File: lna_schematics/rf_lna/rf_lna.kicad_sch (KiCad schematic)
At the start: 18 parts, among them J1 Conn_Coaxial_Small, J2 Conn_Coaxial_Small, U2 BFP640

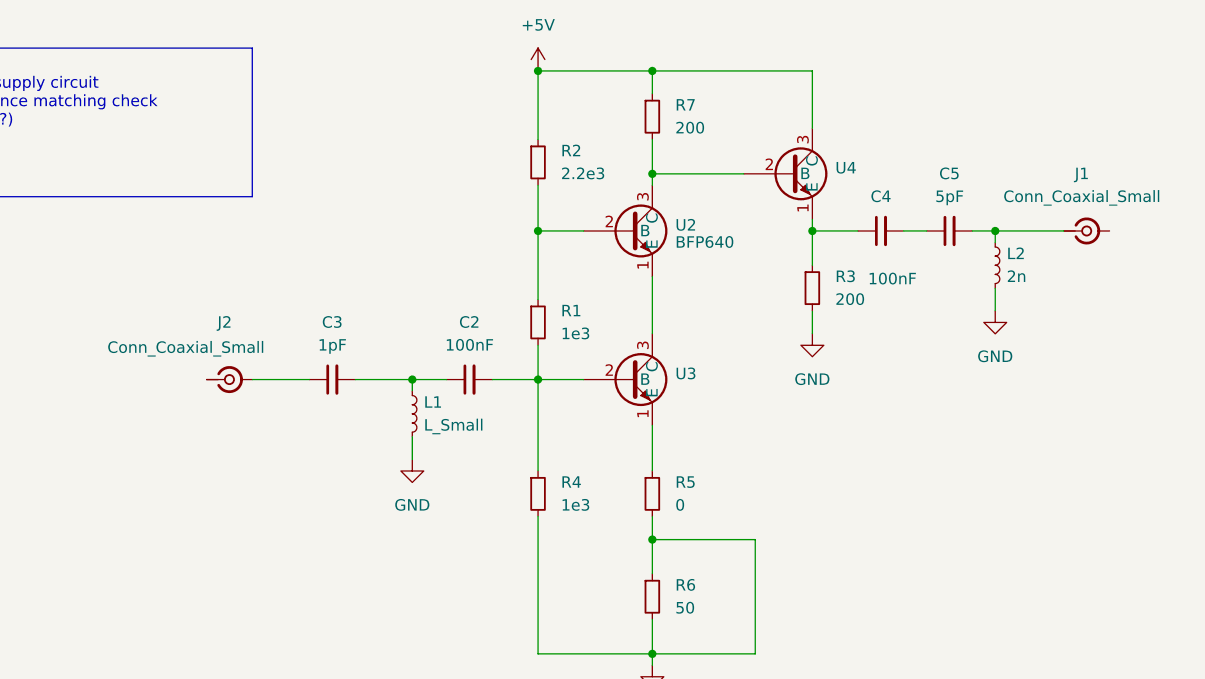
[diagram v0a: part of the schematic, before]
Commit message: [simulations] Added L-matching networks | TODO: find wide-band matching T / Pi matching circuits (800MHz -> 1.5 GHz), find actual working components for the circuit
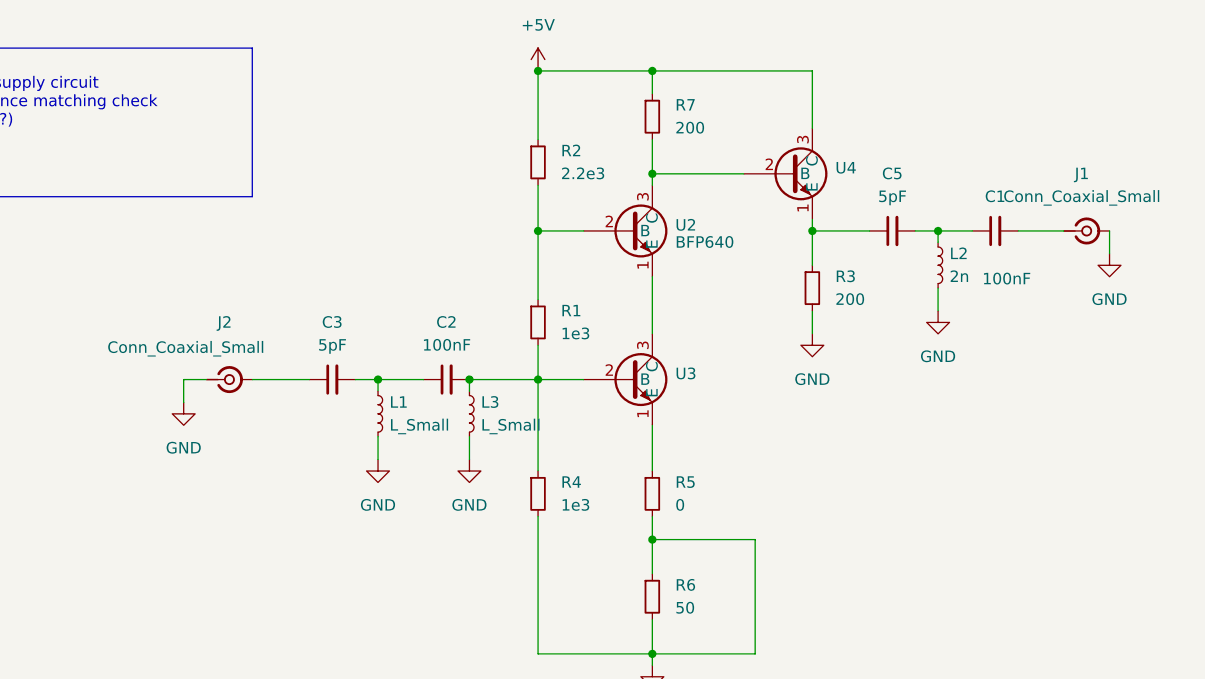
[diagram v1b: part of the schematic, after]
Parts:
- removed C4: 100nF, symbol Device:C_Small
- added C1: 100nF, symbol Device:C_Small
- added L3: L_Small, symbol Device:L_Small
- C3: value 1pF -> 5pF
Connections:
- net GND: now also J1.2 (Ext), J2.1 (In), L3.2
- net at C2.2, R1.2, R4.1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: now also L3.1
- net at R3.1, U4.1 (E): now also C5.1
- net at C5.2, L2.1: now also C1.1; no longer J1.1 (In)
- new net: C1.2, J1.1 (In)
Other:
- moved on the sheet: C2, C5, L1, L2

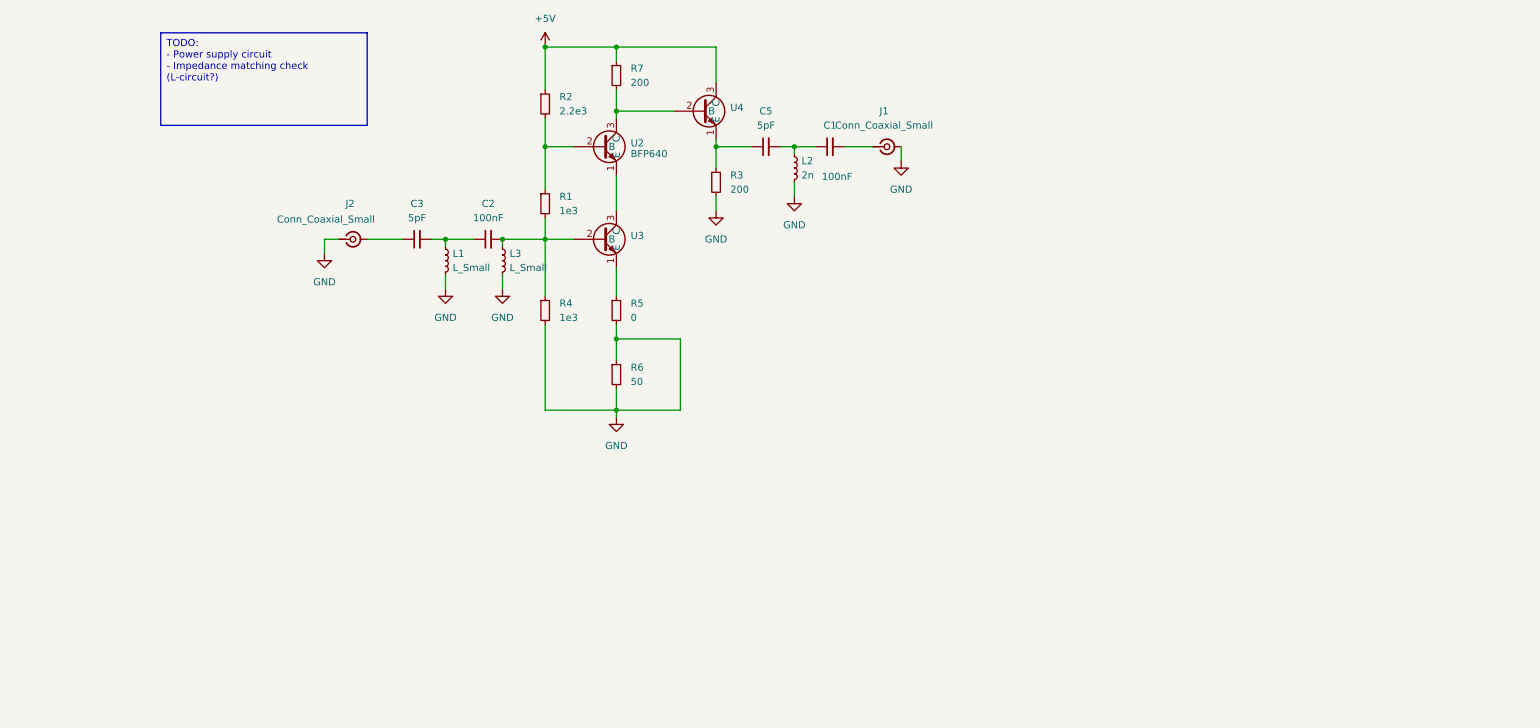
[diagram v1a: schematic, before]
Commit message: [lna_schematics] Simulated with matched impedance to get voltage values and verify matching parameters [lna_schematics] Added matched elements, added notes
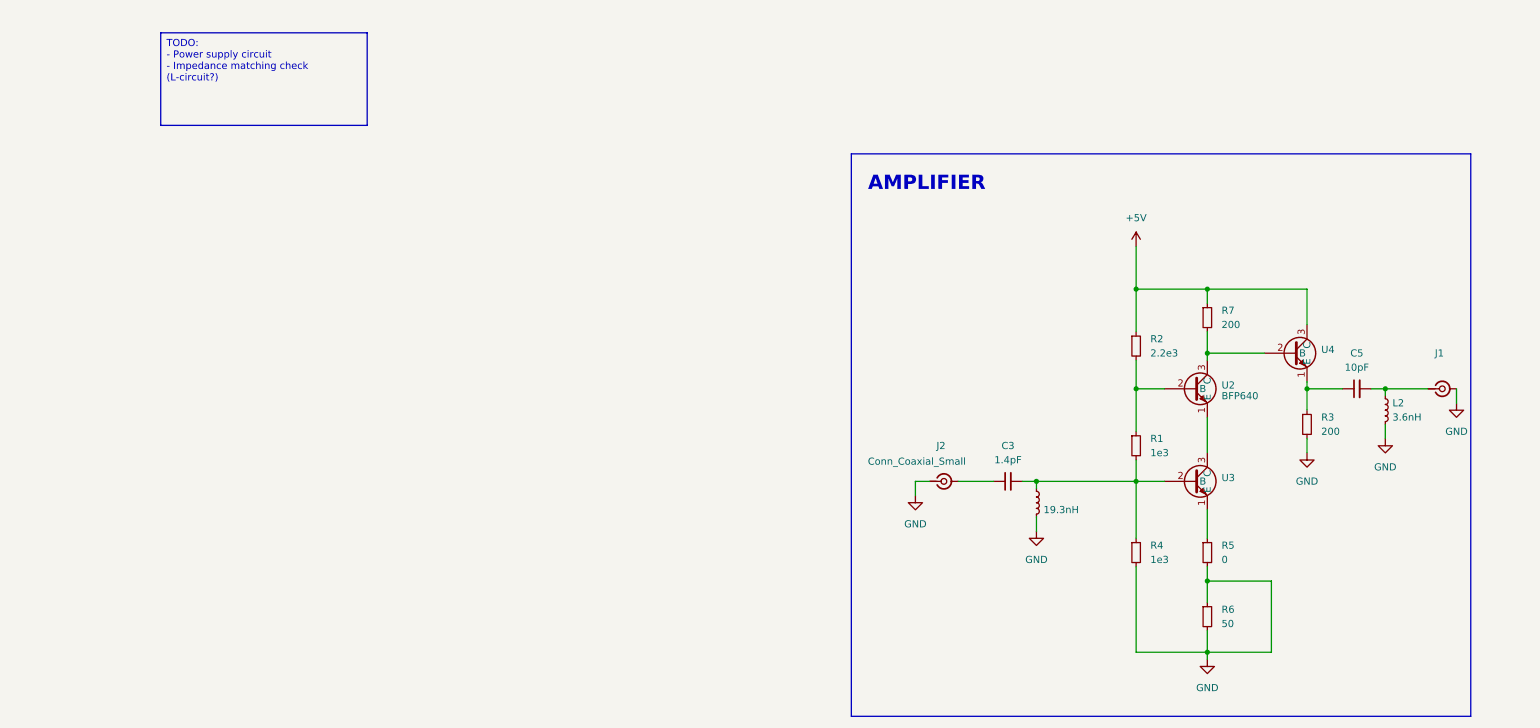
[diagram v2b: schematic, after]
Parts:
- removed C1, C2: 100nF, symbol Device:C_Small
- removed L3: L_Small, symbol Device:L_Small
- C3: value 5pF -> 1.4pF
- C5: value 5pF -> 10pF
- L1: value L_Small -> 19.3nH
- L2: value 2n -> 3.6nH
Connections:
- net at C3.2, L1.1: now also R1.2, R4.1, U3.2 (B)
- net at C5.2, L2.1: now also J1.1 (In)
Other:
- note added: "AMPLIFIER"
- moved on the sheet: C3, C5, J1, J2, L2, R1, R2, R3, R4, R5, R6, R7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

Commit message: [kicad] Added various footprints, added matched network
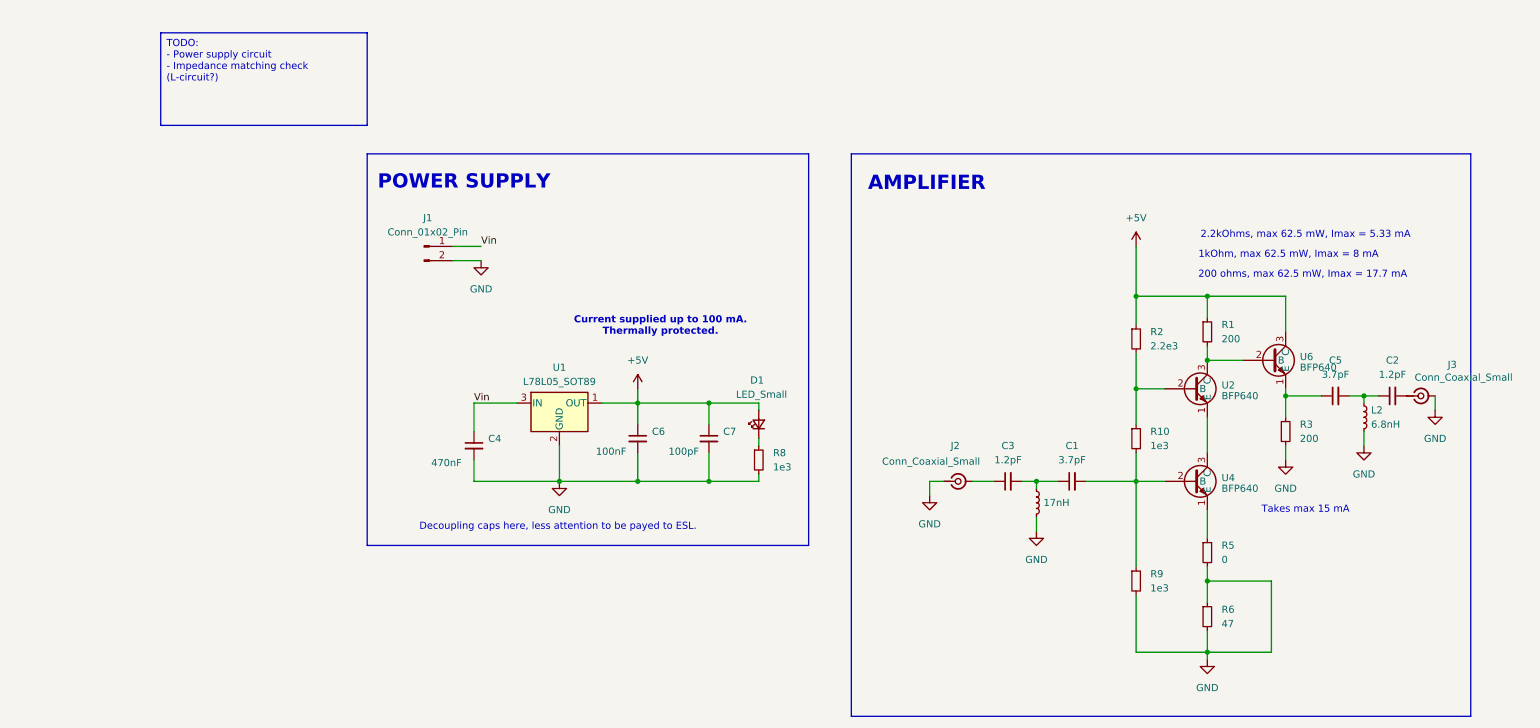
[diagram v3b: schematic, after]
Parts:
- removed J1: Conn_Coaxial_Small, symbol Connector:Conn_Coaxial_Small
- removed R4: 1e3, symbol Device:R_Small
- removed R7: 200, symbol Device:R_Small
- removed U3: ~, symbol rf_lna:BFP640
- added C1: 3.7pF, symbol Device:C_Small
- added C2: 1.2pF, Capacitor_SMD:C_0402_1005Metric, symbol Device:C_Small
- added C4: 470nF, Capacitor_SMD:C_0603_1608Metric, symbol Device:C_Small
- added C6: 100nF, Capacitor_SMD:C_0402_1005Metric, symbol Device:C_Small
- added C7: 100pF, Capacitor_SMD:C_0402_1005Metric, symbol Device:C_Small
- added D1: LED_Small, LED_SMD:LED_0603_1608Metric, symbol Device:LED_Small
- added J1: Conn_01x02_Pin, Connector_Wire:SolderWire-0.25sqmm_1x02_P4.2mm_D0.65mm_OD1.7mm, symbol Connector:Conn_01x02_Pin
- added J3: Conn_Coaxial_Small, Connector_Coaxial:SMA_BAT_Wireless_BWSMA-KWE-Z001, symbol Connector:Conn_Coaxial_Small
- added R10, R8, R9: 1e3, Resistor_SMD:R_0402_1005Metric, symbol Device:R_Small
- added U1: L78L05_SOT89, Package_TO_SOT_SMD:SOT-89-3, symbol Regulator_Linear:L78L05_SOT89
- added U6: BFP640, Library:BFP640, symbol rf_lna:BFP640
- C3: value 1.4pF -> 1.2pF; footprint (none) -> Capacitor_SMD:C_0402_1005Metric; LCSC Part Number (none) -> C76899; Manufacturing Part Number (none) -> GJM1555C1H1R2WB01D
- C5: value 10pF -> 3.7pF
- J2: footprint (none) -> Connector_Coaxial:SMA_BAT_Wireless_BWSMA-KWE-Z001; LCSC Part Number (none) -> C496549; Manufacturing Part Number (none) -> BWSMA-KE-Z001
- L1: value 19.3nH -> 17nH
- L2: value 3.6nH -> 6.8nH
- R1: value 1e3 -> 200; footprint (none) -> Resistor_SMD:R_0402_1005Metric; LCSC Part Number (none) -> C25091; Manufacturing Part Number (none) -> 0402WGF2200TCE
- R2: footprint (none) -> Resistor_SMD:R_0402_1005Metric; LCSC Part Number (none) -> C25879; Manufacturing Part Number (none) -> 0402WGF2201TCE
- R3: footprint (none) -> Resistor_SMD:R_0402_1005Metric; LCSC Part Number (none) -> C25091; Manufacturing Part Number (none) -> 0402WGF2200TCE
- R5: footprint (none) -> Capacitor_SMD:C_0402_1005Metric; LCSC Part Number (none) -> C17168; Manufacturing Part Number (none) -> 0402WGF0000TCE
- R6: value 50 -> 47; footprint (none) -> Capacitor_SMD:C_0402_1005Metric; LCSC Part Number (none) -> C4109; Manufacturing Part Number (none) -> 0402WGF2001TCE
- U2: footprint (none) -> Library:BFP640; LCSC Part Number (none) -> C439781; MFR.Part BFP640H6327 -> (none); Manufacturing Part Number (none) -> BFP640H6327; jlcpcb C439781 -> (none)
- U4: value ~ -> BFP640; footprint (none) -> Library:BFP640; LCSC Part Number (none) -> C439781; Manufacturing Part Number (none) -> BFP640H6327
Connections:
- net +5V: now also R1.1, C6.1, C7.1, D1.2 (A), U1.1 (OUT), U6.3 (C); no longer U4.3 (C)
- net GND: now also C4.2, C6.2, C7.2, J1.2 (Pin_2), J3.2 (Ext), R8.2, R9.2, U1.2 (GND)
- net at C3.2, L1.1: now also C1.1; no longer R1.2
- net at C5.1, R3.1: now also U6.1 (E); no longer U4.1 (E)
- net at U4.2 (B): now also C1.2, R10.2, R9.1; no longer U2.3 (C)
- net at R5.1: now also U4.1 (E)
- net at C5.2, L2.1: now also C2.1
- net at R2.2, U2.2 (B): now also R10.1; no longer R1.1
- net at U2.1 (E): now also U4.3 (C)
- new net: D1.1 (K), R8.1
- new net: C2.2, J3.1 (In)
- new net: R1.2, U2.3 (C), U6.2 (B)
- new net Vin: C4.1, J1.1 (Pin_1), U1.3 (IN)
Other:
- note added: "1kOhm, max 62.5 mW, Imax = 8 mA"
- note added: "2.2kOhms, max 62.5 mW, Imax = 5.33 mA"
- note added: "200 ohms, max 62.5 mW, Imax = 17.7 mA"
- note added: "Current supplied up to 100 mA. Thermally protected."
- note added: "Decoupling caps here, less attention to be payed to ESL."
- note added: "POWER SUPPLY"
- note added: "Takes max 15 mA"
- moved on the sheet: C5, J2, L2, R2, R3

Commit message: [lna_schematics] added final components for impedance matching [simulations] Added final impedance matched simulations | TODO: stackup + layout + footprint check
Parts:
- C1, C5: footprint (none) -> Capacitor_SMD:C_0402_1005Metric; LCSC Part Number (none) -> C161321; Manufacturing Part Number (none) -> GJM1555C1H3R6WB01D
- L1: value 17nH -> 18nH; footprint (none) -> Inductor_SMD:L_0402_1005Metric; LCSC Part Number (none) -> C24562; Manufacturing Part Number (none) -> SDCL1005C18NJTDF
- L2: footprint (none) -> Inductor_SMD:L_0402_1005Metric; LCSC Part Number (none) -> C32041; Manufacturing Part Number (none) -> SDCL1005C6N8JTDF

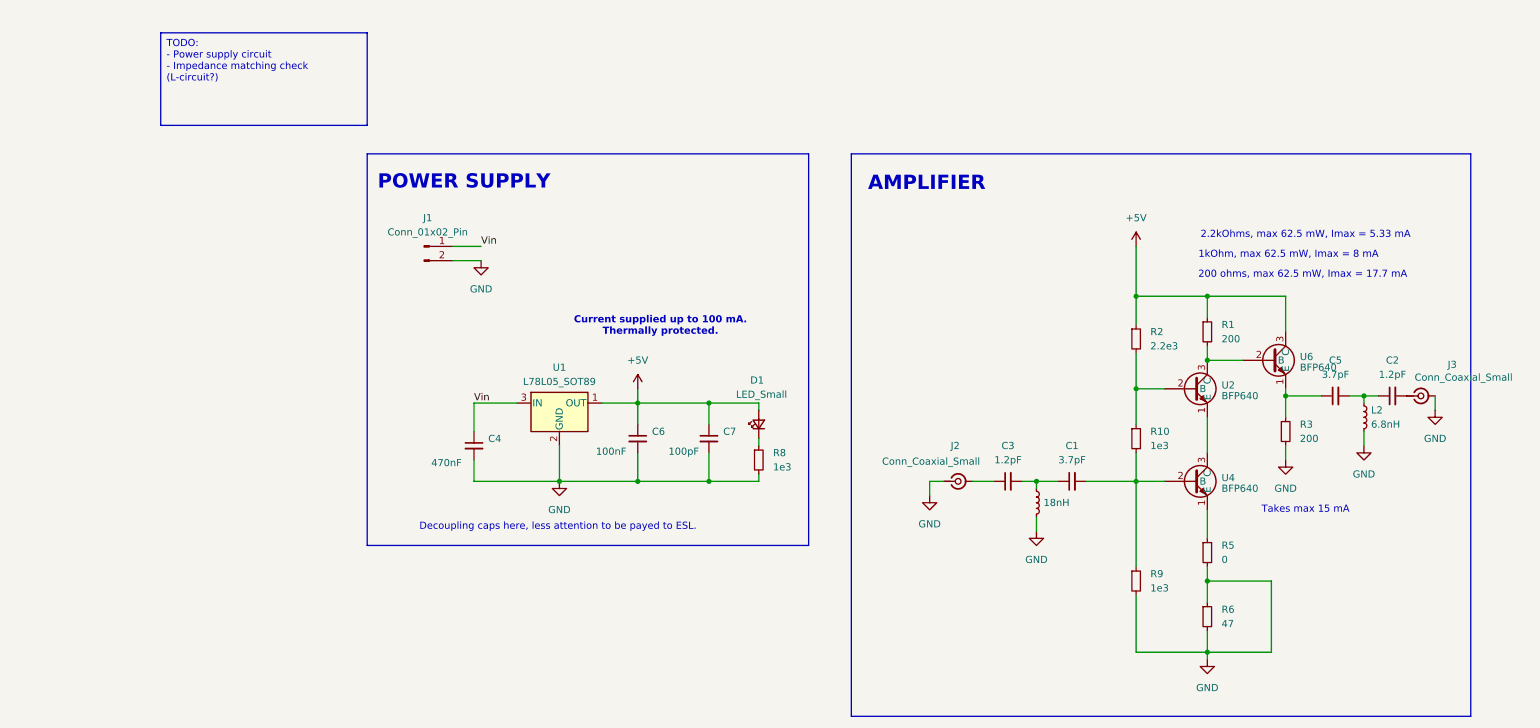
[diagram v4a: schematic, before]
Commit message: [kicad] Finished pads, stackup, symbols for LNA. Starting layout.
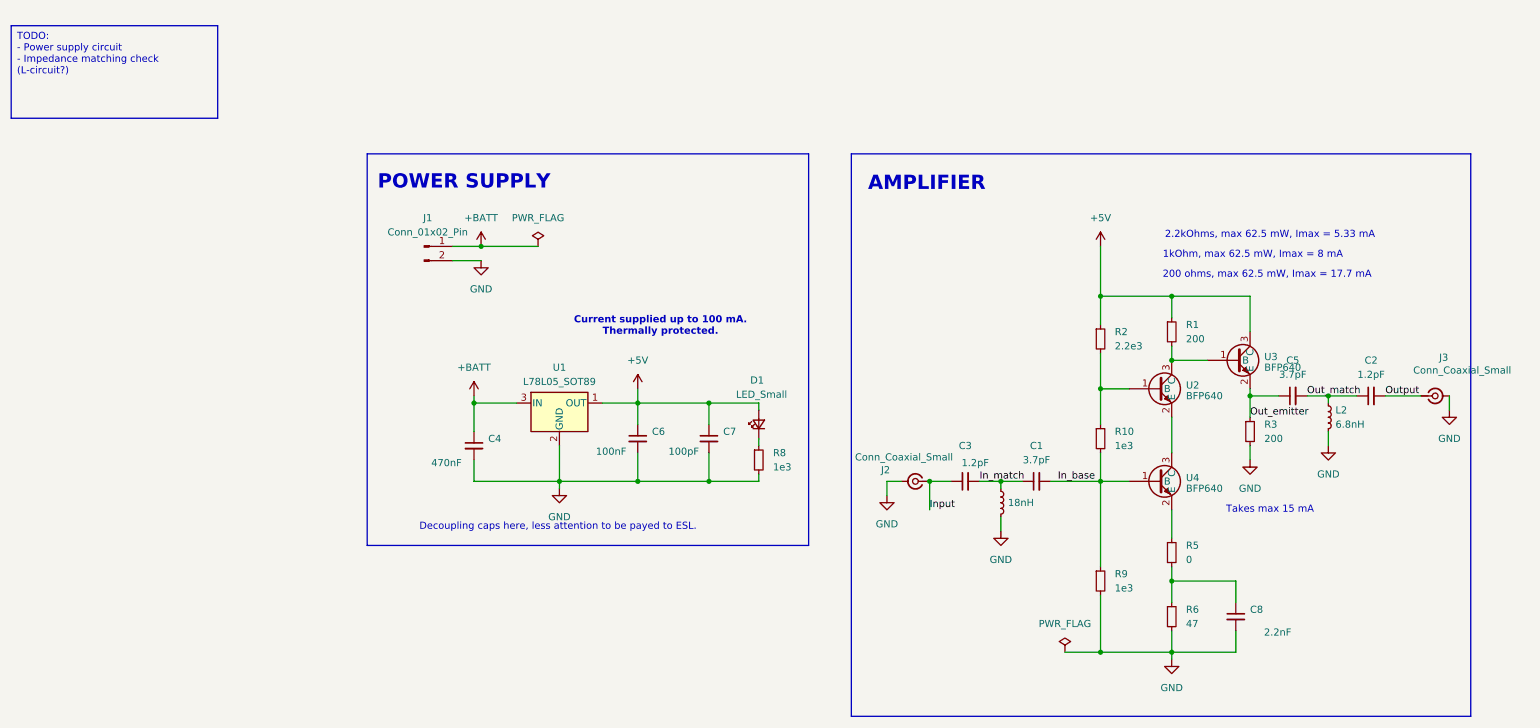
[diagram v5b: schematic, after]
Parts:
- removed U6: BFP640, Library:BFP640, symbol rf_lna:BFP640
- added C8: 2.2nF, Capacitor_SMD:C_0805_2012Metric, symbol Device:C_Small
- added U3: BFP640, Library:BFP640, symbol rf_lna:BFP640
- J2, J3: footprint Connector_Coaxial:SMA_BAT_Wireless_BWSMA-KWE-Z001 -> Library:SMA_Amphenol_901-143_Vertical
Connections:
- net +5V: now also U3.3 (C)
- net GND: now also J2.2 (Ext), C8.2; no longer J2.1 (In), R5.2, R6.1
- net Input: now reaches C3.1
- net Input: now also J2.1 (In); no longer J2.2 (Ext)
- net In_match: now reaches C1.1, C3.2, L1.1
- net at R5.1: now also U4.2 (E); no longer U4.1 (E)
- net In_base: now reaches C1.2, R10.2, R9.1
- net In_base: now also U4.1 (B); no longer U4.2 (B)
- net Output: now reaches C2.2, J3.1 (In)
- net at R1.2, U2.3 (C): now also U3.1 (B)
- net Out_match: now reaches C2.1, C5.2, L2.1
- net Out_emitter: now reaches C5.1, R3.1
- net Out_emitter: now also U3.2 (E)
- net at U2.1 (B): now also R10.1, R2.2; no longer U4.3 (C)
- net Vin renamed +BATT
- new net: C8.1, R5.2, R6.1
- new net: U2.2 (E), U4.3 (C)
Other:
- moved on the sheet: C1, C2, C3, C5, J3, L2, R1, R10, R2, R3, R5, R6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
